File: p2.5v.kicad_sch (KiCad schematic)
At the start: 11 parts, among them U13 LT3045xDD

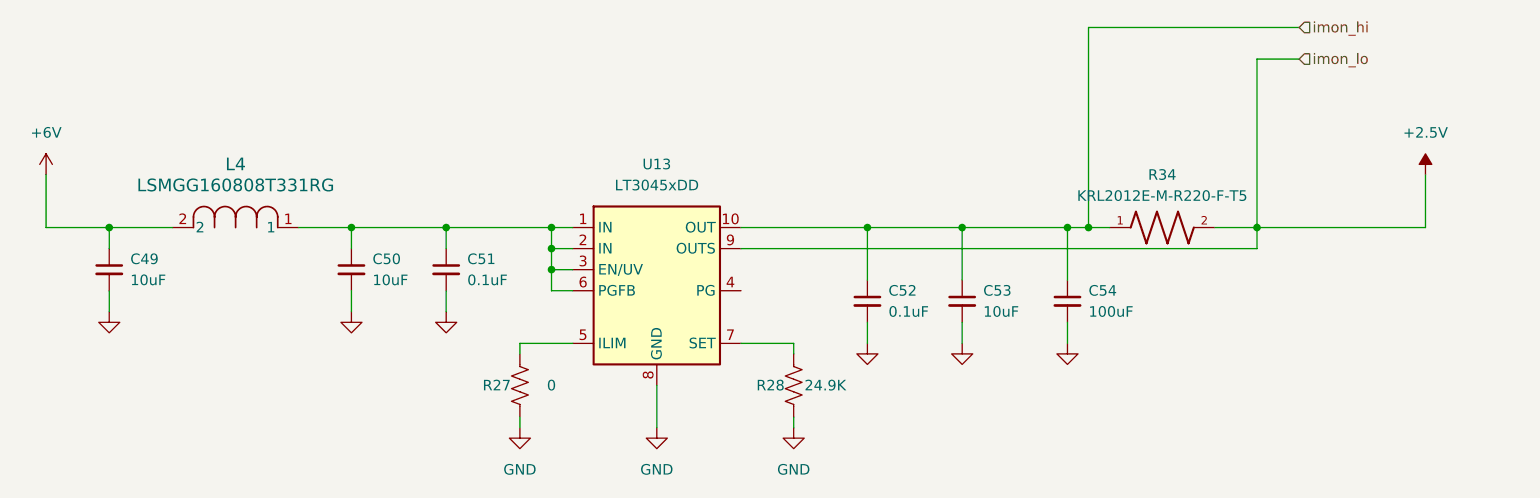
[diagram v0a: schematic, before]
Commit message: Add all 4 channels
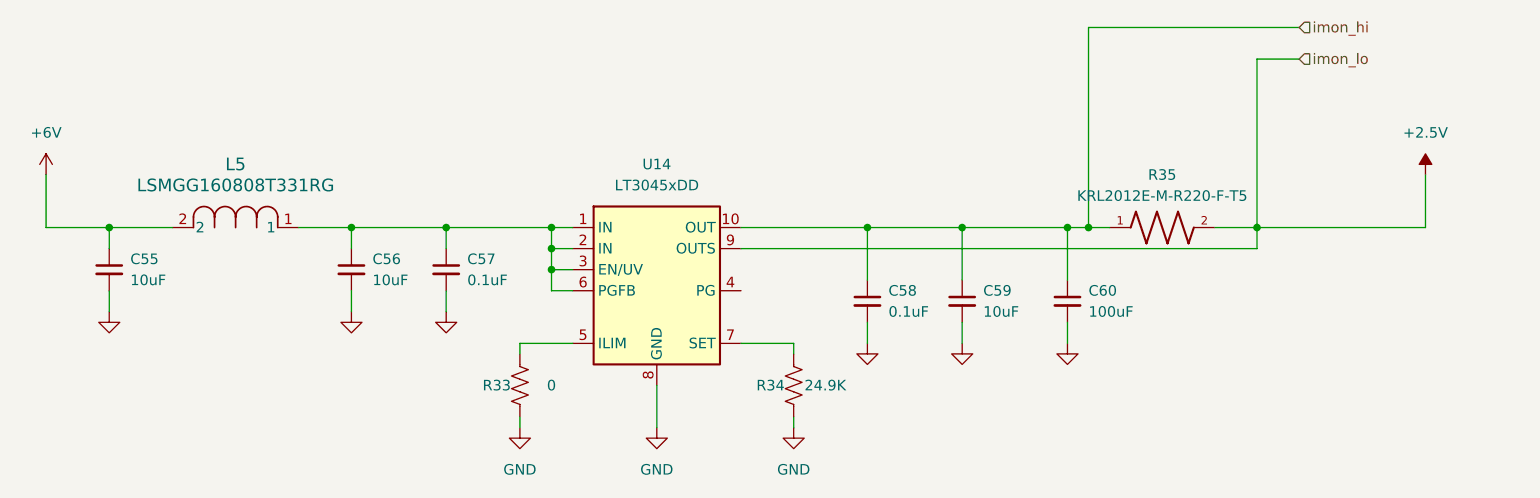
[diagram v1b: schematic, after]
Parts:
- renumbered C49 to C55, C50 to C56, C51 to C57, C52 to C58, C53 to C59, C54 to C60, L4 to L5, R27 to R33, R28 to R34, R34 to R35, U13 to U14
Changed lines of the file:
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@@
 		(dnp no)
 		(fields_autoplaced yes)
-		(property "Reference" "#PWR0119"
+		(property "Reference" "#PWR0135"
 			(at 181.61 91.44 0)
 			(effects
@@
 			(project "psc_carrier_brd"
 				(path "/40891cc8-bf64-41f4-8f69-a607d7b280eb/d1842e08-6ad7-4891-bdb3-3a3a498e2a30/4d03c65a-11e6-4d8a-8956-a18576278712"
-					(reference "#PWR0119")
+					(reference "#PWR0135")
 					(unit 1)
 				)
@@
 		(on_board yes)
 		(dnp no)
-		(property "Reference" "C49"
+		(property "Reference" "C55"
 			(at 81.28 74.9362 0)
 			(effects
@@
 			(project "psc_carrier_brd"
 				(path "/40891cc8-bf64-41f4-8f69-a607d7b280eb/d1842e08-6ad7-4891-bdb3-3a3a498e2a30/4d03c65a-11e6-4d8a-8956-a18576278712"
-					(reference "C49")
+					(reference "C55")
 					(unit 1)
 				)
@@
 		(on_board yes)
 		(dnp no)
-		(property "Reference" "C54"
+		(property "Reference" "C60"
 			(at 196.85 78.7462 0)
 			(effects
@@
 			(project "psc_carrier_brd"
 				(path "/40891cc8-bf64-41f4-8f69-a607d7b280eb/d1842e08-6ad7-4891-bdb3-3a3a498e2a30/4d03c65a-11e6-4d8a-8956-a18576278712"
-					(reference "C54")
+					(reference "C60")
 					(unit 1)
 				)
@@
 		(on_board yes)
 		(dnp no)
-		(property "Reference" "R27"
+		(property "Reference" "R33"
 			(at 125.476 90.17 0)
 			(effects
@@
 			(project "psc_carrier_brd"
 				(path "/40891cc8-bf64-41f4-8f69-a607d7b280eb/d1842e08-6ad7-4891-bdb3-3a3a498e2a30/4d03c65a-11e6-4d8a-8956-a18576278712"
-					(reference "R27")
+					(reference "R33")
 					(unit 1)
 				)
@@
 		(dnp no)
 		(fields_autoplaced yes)
-		(property "Reference" "#PWR0121"
+		(property "Reference" "#PWR0137"
 			(at 237.49 68.58 0)
 			(effects
@@
 			(project ""
 				(path "/40891cc8-bf64-41f4-8f69-a607d7b280eb/d1842e08-6ad7-4891-bdb3-3a3a498e2a30/4d03c65a-11e6-4d8a-8956-a18576278712"
-					(reference "#PWR0121")
+					(reference "#PWR0137")
 					(unit 1)
 				)
@@
 		(on_board yes)
 		(dnp no)
-		(property "Reference" "C52"
+		(property "Reference" "C58"
 			(at 172.72 78.7462 0)
 			(effects
@@
 			(project "psc_carrier_brd"
 				(path "/40891cc8-bf64-41f4-8f69-a607d7b280eb/d1842e08-6ad7-4891-bdb3-3a3a498e2a30/4d03c65a-11e6-4d8a-8956-a18576278712"
-					(reference "C52")
+					(reference "C58")
 					(unit 1)
 				)
@@
 		(dnp no)
 		(fields_autoplaced yes)
-		(property "Reference" "#PWR0118"
+		(property "Reference" "#PWR0134"
 			(at 170.18 91.44 0)
 			(effects
@@
 			(project "psc_carrier_brd"
 				(path "/40891cc8-bf64-41f4-8f69-a607d7b280eb/d1842e08-6ad7-4891-bdb3-3a3a498e2a30/4d03c65a-11e6-4d8a-8956-a18576278712"
-					(reference "#PWR0118")
+					(reference "#PWR0134")
 					(unit 1)
 				)
@@
 		(dnp no)
 		(fields_autoplaced yes)
-		(property "Reference" "#PWR0111"
+		(property "Reference" "#PWR0127"
 			(at 71.12 68.58 0)
 			(effects
@@
 				)
 				(path "/40891cc8-bf64-41f4-8f69-a607d7b280eb/d1842e08-6ad7-4891-bdb3-3a3a498e2a30/4d03c65a-11e6-4d8a-8956-a18576278712"
-					(reference "#PWR0111")
+					(reference "#PWR0127")
 					(unit 1)
 				)
@@
 		(dnp no)
 		(fields_autoplaced yes)
-		(property "Reference" "U13"
+		(property "Reference" "U14"
 			(at 144.78 63.5 0)
 			(effects
@@
 				)
 				(path "/40891cc8-bf64-41f4-8f69-a607d7b280eb/d1842e08-6ad7-4891-bdb3-3a3a498e2a30/4d03c65a-11e6-4d8a-8956-a18576278712"
-					(reference "U13")
+					(reference "U14")
 					(unit 1)
 				)
@@
 		(on_board yes)
 		(dnp no)
-		(property "Reference" "C50"
+		(property "Reference" "C56"
 			(at 110.49 74.9362 0)
 			(effects
@@
 			(project "psc_carrier_brd"
 				(path "/40891cc8-bf64-41f4-8f69-a607d7b280eb/d1842e08-6ad7-4891-bdb3-3a3a498e2a30/4d03c65a-11e6-4d8a-8956-a18576278712"
-					(reference "C50")
+					(reference "C56")
 					(unit 1)
 				)
@@
 		(on_board yes)
 		(dnp no)
-		(property "Reference" "C53"
+		(property "Reference" "C59"
 			(at 184.15 78.7462 0)
 			(effects
@@
 			(project "psc_carrier_brd"
 				(path "/40891cc8-bf64-41f4-8f69-a607d7b280eb/d1842e08-6ad7-4891-bdb3-3a3a498e2a30/4d03c65a-11e6-4d8a-8956-a18576278712"
-					(reference "C53")
+					(reference "C59")
 					(unit 1)
 				)
@@
 		(on_board yes)
 		(dnp no)
-		(property "Reference" "C51"
+		(property "Reference" "C57"
 			(at 121.92 74.9362 0)
 			(effects
@@
 			(project "psc_carrier_brd"
 				(path "/40891cc8-bf64-41f4-8f69-a607d7b280eb/d1842e08-6ad7-4891-bdb3-3a3a498e2a30/4d03c65a-11e6-4d8a-8956-a18576278712"
-					(reference "C51")
+					(reference "C57")
 					(unit 1)
 				)
@@
 		(dnp no)
 		(fields_autoplaced yes)
-		(property "Reference" "R34"
+		(property "Reference" "R35"
 			(at 205.74 64.77 0)
 			(effects
@@
 			(project "psc_carrier_brd"
 				(path "/40891cc8-bf64-41f4-8f69-a607d7b280eb/d1842e08-6ad7-4891-bdb3-3a3a498e2a30/4d03c65a-11e6-4d8a-8956-a18576278712"
-					(reference "R34")
+					(reference "R35")
 					(unit 1)
 				)
@@
 		(dnp no)
 		(fields_autoplaced yes)
-		(property "Reference" "#PWR0112"
+		(property "Reference" "#PWR0128"
 			(at 78.74 87.63 0)
 			(effects
@@
 			(project "psc_carrier_brd"
 				(path "/40891cc8-bf64-41f4-8f69-a607d7b280eb/d1842e08-6ad7-4891-bdb3-3a3a498e2a30/4d03c65a-11e6-4d8a-8956-a18576278712"
-					(reference "#PWR0112")
+					(reference "#PWR0128")
 					(unit 1)
 				)
@@
 		(dnp no)
 		(fields_autoplaced yes)
-		(property "Reference" "L4"
+		(property "Reference" "L5"
 			(at 93.98 63.5 0)
 			(effects
@@
 				)
 				(path "/40891cc8-bf64-41f4-8f69-a607d7b280eb/d1842e08-6ad7-4891-bdb3-3a3a498e2a30/4d03c65a-11e6-4d8a-8956-a18576278712"
-					(reference "L4")
+					(reference "L5")
 					(unit 1)
 				)
@@
 		(dnp no)
 		(fields_autoplaced yes)
-		(property "Reference" "#PWR0117"
+		(property "Reference" "#PWR0133"
 			(at 161.29 101.6 0)
 			(effects
@@
 			(project "psc_carrier_brd"
 				(path "/40891cc8-bf64-41f4-8f69-a607d7b280eb/d1842e08-6ad7-4891-bdb3-3a3a498e2a30/4d03c65a-11e6-4d8a-8956-a18576278712"
-					(reference "#PWR0117")
+					(reference "#PWR0133")
 					(unit 1)
 				)
@@
 		(dnp no)
 		(fields_autoplaced yes)
-		(property "Reference" "#PWR0120"
+		(property "Reference" "#PWR0136"
 			(at 194.31 91.44 0)
 			(effects
@@
 			(project "psc_carrier_brd"
 				(path "/40891cc8-bf64-41f4-8f69-a607d7b280eb/d1842e08-6ad7-4891-bdb3-3a3a498e2a30/4d03c65a-11e6-4d8a-8956-a18576278712"
-					(reference "#PWR0120")
+					(reference "#PWR0136")
 					(unit 1)
 				)
@@
 		(dnp no)
 		(fields_autoplaced yes)
-		(property "Reference" "#PWR0113"
+		(property "Reference" "#PWR0129"
 			(at 107.95 87.63 0)
 			(effects
@@
 			(project "psc_carrier_brd"
 				(path "/40891cc8-bf64-41f4-8f69-a607d7b280eb/d1842e08-6ad7-4891-bdb3-3a3a498e2a30/4d03c65a-11e6-4d8a-8956-a18576278712"
-					(reference "#PWR0113")
+					(reference "#PWR0129")
 					(unit 1)
 				)
@@
 		(dnp no)
 		(fields_autoplaced yes)
-		(property "Reference" "#PWR0114"
+		(property "Reference" "#PWR0130"
 			(at 119.38 87.63 0)
 			(effects
@@
 			(project "psc_carrier_brd"
 				(path "/40891cc8-bf64-41f4-8f69-a607d7b280eb/d1842e08-6ad7-4891-bdb3-3a3a498e2a30/4d03c65a-11e6-4d8a-8956-a18576278712"
-					(reference "#PWR0114")
+					(reference "#PWR0130")
 					(unit 1)
 				)
@@
 		(dnp no)
 		(fields_autoplaced yes)
-		(property "Reference" "#PWR0116"
+		(property "Reference" "#PWR0132"
 			(at 144.78 101.6 0)
 			(effects
@@
 				)
 				(path "/40891cc8-bf64-41f4-8f69-a607d7b280eb/d1842e08-6ad7-4891-bdb3-3a3a498e2a30/4d03c65a-11e6-4d8a-8956-a18576278712"
-					(reference "#PWR0116")
+					(reference "#PWR0132")
 					(unit 1)
 				)
@@
 		(on_board yes)
 		(dnp no)
-		(property "Reference" "R28"
+		(property "Reference" "R34"
 			(at 158.496 90.17 0)
 			(effects
@@
 			(project "psc_carrier_brd"
 				(path "/40891cc8-bf64-41f4-8f69-a607d7b280eb/d1842e08-6ad7-4891-bdb3-3a3a498e2a30/4d03c65a-11e6-4d8a-8956-a18576278712"
-					(reference "R28")
+					(reference "R34")
 					(unit 1)
 				)
@@
 		(dnp no)
 		(fields_autoplaced yes)
-		(property "Reference" "#PWR0115"
+		(property "Reference" "#PWR0131"
 			(at 128.27 101.6 0)
 			(effects
@@
 			(project "psc_carrier_brd"
 				(path "/40891cc8-bf64-41f4-8f69-a607d7b280eb/d1842e08-6ad7-4891-bdb3-3a3a498e2a30/4d03c65a-11e6-4d8a-8956-a18576278712"
-					(reference "#PWR0115")
-					(unit 1)
-				)
+					(reference "#PWR0131")
+					(unit 1)
+				)

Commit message: Start routing
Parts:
- renumbered C55 to C40, C56 to C41, C57 to C42, C58 to C43, C59 to C44, C60 to C45, R33 to R23, R34 to R24, R35 to R25, U14 to U10
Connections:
- net +6V renamed +5.0V
- no-connect marks 0 -> 1

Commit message: Finished layout
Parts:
- added TP7: ${SHORT_NET_NAME(1)}, TestPoint:TestPoint_THTPad_D2.0mm_Drill1.0mm, symbol Connector:TestPoint
- C40, C41, C44: Cost (none) -> .04; MFG (none) -> Samsung; MFG_PN (none) -> CL10A106MA8NRNC
- C42, C43: Cost (none) -> .01; MFG (none) -> Taiyo Yuden; MFG_PN (none) -> TMK105BJ104KV-F
- C45: Cost (none) -> 0.22; MFG (none) -> Murata; MFG_PN (none) -> GRM31CR61A107MEA8L
- L5: Cost (none) -> .01; MFG (none) -> Taiyo Yuden; MFG_PN (none) -> LSMGG160808T331RG
- R23: Cost (none) -> 0.01; MFG (none) -> Panasonic; MFG_PN (none) -> ERJ-2GE0R00X
- R24: Cost (none) -> 0.01; MFG (none) -> Panasonic; MFG_PN (none) -> ERJ-2RKF2492X
- R25: value KRL2012E-M-R220-F-T5 -> 0.22; Cost (none) -> 0.38; MFG (none) -> Susumu; MFG_PN (none) -> KRL2012E-M-R220-F-T5
- U10: Cost (none) -> 6.06; MFG (none) -> Analog Devices; MFG_PN (none) -> LT3045EDD#TRPBF
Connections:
- net +2.5V: now also TP7.1
- net Vin_2.5v: now reaches C41.1, C42.1, L5.1, U10.1 (IN), U10.2 (IN), U10.6 (PGFB)
- net Vin_2.5v: no longer U10.3 (EN/UV)
- new net enb: U10.3 (EN/UV)
